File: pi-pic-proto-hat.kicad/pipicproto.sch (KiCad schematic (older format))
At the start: 27 parts, among them J1 RUN/~PGM~, J10 Conn_01x13_Male, J2 Conn_SW1, J22 Conn_01x13_Male, J3 Conn_01x05_Male, J6 Barrel_Jack_Switch, J7 Conn_01x24_Male, J8 Conn_01x06_Male, J9 Conn_01x02_Male, P1 Conn_02x20_Odd_Even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

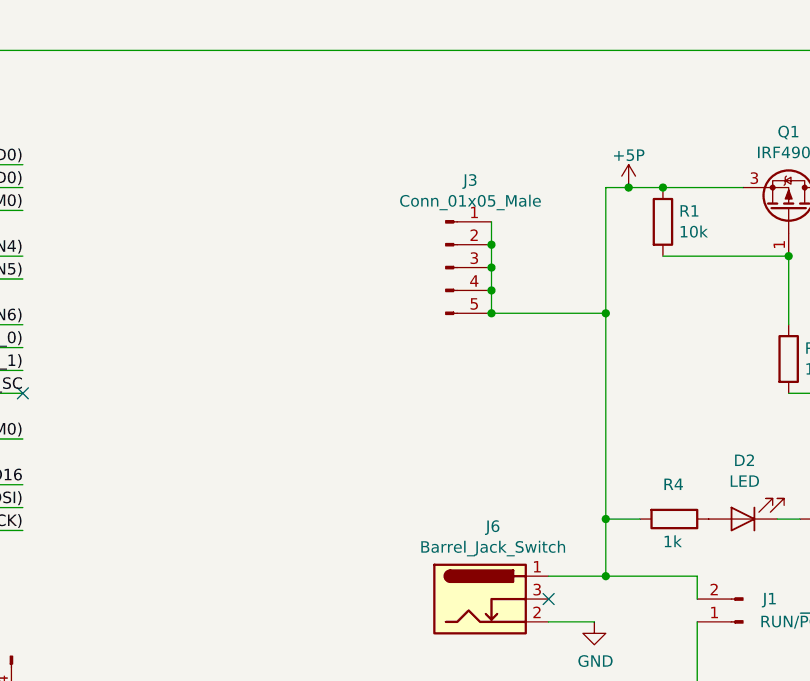
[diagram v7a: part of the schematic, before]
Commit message: V2.16: added regulator and connector for +3V3P (3V3 permanently on)
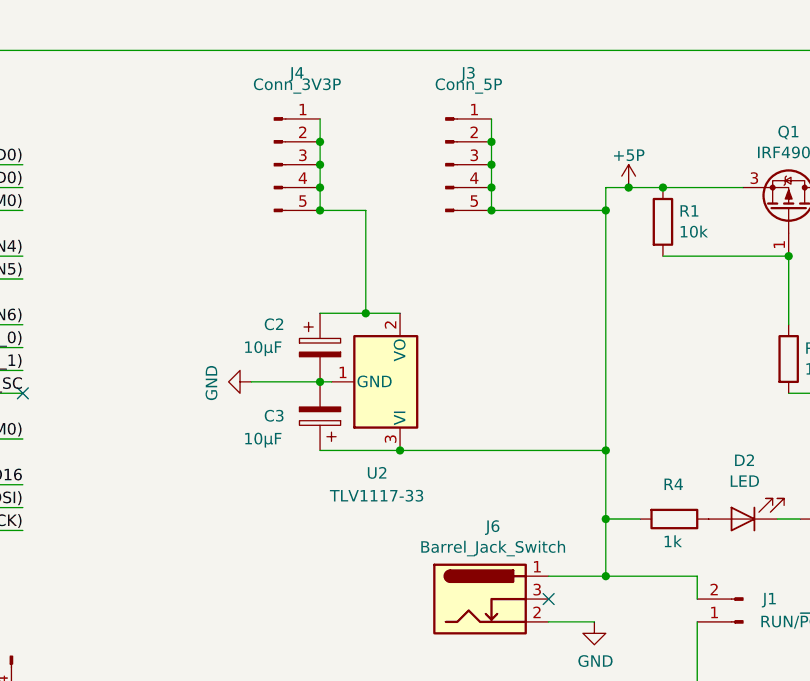
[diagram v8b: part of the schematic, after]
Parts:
- added C2, C3: 10µF, Capacitor_Tantalum_SMD:CP_EIA-3216-18_Kemet-A, symbol Device:CP
- added J4: Conn_3V3P, Connector_PinHeader_2.54mm:PinHeader_1x05_P2.54mm_Vertical, symbol Connector:Conn_01x05_Male
- added U2: TLV1117-33, Package_TO_SOT_SMD:SOT-223, symbol Regulator_Linear:TLV1117-33
- J3: value Conn_01x05_Male -> Conn_5P
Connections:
- net +5P: now also C3.1, U2.3 (VI)
- net GND: now also C2.2, C3.2, U2.1 (GND)
- new net: C2.1, J4.1 (Pin_1), J4.2 (Pin_2), J4.3 (Pin_3), J4.4 (Pin_4), J4.5 (Pin_5), U2.2 (VO)
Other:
- moved on the sheet: J3
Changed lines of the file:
@@
 Title "PI PIC Prototyping Area"
 Date "2020-07-24"
-Rev "2.15"
+Rev "2.16"
 Comp "Bernhard Bablok, Lothar Hiller"
 Comment1 "https://github.com/bablokb/pi-pic-proto-hat"
@@
 	6900 3400 6900 4300
 Wire Wire Line
-	6500 1500 6500 2050
+	6500 1500 6500 1600
 Wire Wire Line
 	6500 3200 6900 3200
@@
 L Connector:Conn_01x05_Male J3
 U 1 1 5F1C34FF
-P 5800 1850
-F 0 "J3" H 5908 2231 50  0000 C CNN
-F 1 "Conn_01x05_Male" H 5908 2140 50  0000 C CNN
-F 2 "Connector_PinHeader_2.54mm:PinHeader_1x05_P2.54mm_Vertical" H 5800 1850 50  0001 C CNN
-F 3 "~" H 5800 1850 50  0001 C CNN
-	1    5800 1850
-	1    0    0    -1
-$EndComp
-Wire Wire Line
-	6500 2050 6000 2050
-Wire Wire Line
-	6000 2050 6000 1950
-Connection ~ 6500 2050
-Wire Wire Line
-	6500 2050 6500 2950
-Connection ~ 6000 2050
-Wire Wire Line
-	6000 1850 6000 1750
-Wire Wire Line
-	6000 1950 6000 1850
-Connection ~ 6000 1950
-Connection ~ 6000 1850
-Wire Wire Line
-	6000 1750 6000 1650
-Connection ~ 6000 1750
+P 5800 1400
+F 0 "J3" H 5900 1800 50  0000 C CNN
+F 1 "Conn_5P" H 5900 1750 50  0000 C CNN
+F 2 "Connector_PinHeader_2.54mm:PinHeader_1x05_P2.54mm_Vertical" H 5800 1400 50  0001 C CNN
+F 3 "~" H 5800 1400 50  0001 C CNN
+	1    5800 1400
+	1    0    0    -1
+$EndComp
+Wire Wire Line
+	6500 1600 6000 1600
+Wire Wire Line
+	6000 1600 6000 1500
+Connection ~ 6000 1600
+Wire Wire Line
+	6000 1400 6000 1300
+Wire Wire Line
+	6000 1500 6000 1400
+Connection ~ 6000 1500
+Connection ~ 6000 1400
+Wire Wire Line
+	6000 1300 6000 1200
+Connection ~ 6000 1300
+$Comp
+L power:GND #PWR09
+U 1 1 5F1C3E14
+P 4950 2350
+F 0 "#PWR09" H 4950 2100 50  0001 C CNN
+F 1 "GND" H 4955 2177 50  0000 C CNN
+F 2 "" H 4950 2350 50  0001 C CNN
+F 3 "" H 4950 2350 50  0001 C CNN
+	1    4950 2350
+	0    1    1    0
+$EndComp
+Wire Wire Line
+	5300 2350 5250 2350
+$Comp
+L Device:CP C2
+U 1 1 5F1C3E1B
+P 5250 2200
+F 0 "C2" H 5050 2300 50  0000 C CNN
+F 1 "10µF" H 5000 2200 50  0000 C CNN
+F 2 "Capacitor_Tantalum_SMD:CP_EIA-3216-18_Kemet-A" H 5288 2050 50  0001 C CNN
+F 3 "~" H 5250 2200 50  0001 C CNN
+	1    5250 2200
+	1    0    0    -1
+$EndComp
+Connection ~ 5250 2350
+Wire Wire Line
+	5250 2350 4950 2350
+$Comp
+L Device:CP C3
+U 1 1 5F1C3E29
+P 5250 2500
+F 0 "C3" H 5450 2500 50  0000 C CNN
+F 1 "10µF" H 5500 2600 50  0000 C CNN
+F 2 "Capacitor_Tantalum_SMD:CP_EIA-3216-18_Kemet-A" H 5288 2350 50  0001 C CNN
+F 3 "~" H 5250 2500 50  0001 C CNN
+	1    5250 2500
+	-1   0    0    1
+$EndComp
+Wire Wire Line
+	5250 2050 5450 2050
+Connection ~ 6500 1600
+Wire Wire Line
+	6500 1600 6500 2650
+Connection ~ 6500 2650
+Wire Wire Line
+	6500 2650 6500 2950
+$Comp
+L Connector:Conn_01x05_Male J4
+U 1 1 5F1D5F8D
+P 5050 1400
+F 0 "J4" H 5150 1800 50  0000 C CNN
+F 1 "Conn_3V3P" H 5150 1750 50  0000 C CNN
+F 2 "Connector_PinHeader_2.54mm:PinHeader_1x05_P2.54mm_Vertical" H 5050 1400 50  0001 C CNN
+F 3 "~" H 5050 1400 50  0001 C CNN
+	1    5050 1400
+	1    0    0    -1
+$EndComp
+Wire Wire Line
+	5450 2050 5450 1600
+Wire Wire Line
+	5450 1600 5250 1600
+Connection ~ 5450 2050
+Wire Wire Line
+	5450 2050 5600 2050
+Wire Wire Line
+	5250 1600 5250 1500
+Connection ~ 5250 1600
+Wire Wire Line
+	5250 1500 5250 1400
+Connection ~ 5250 1500
+Wire Wire Line
+	5250 1400 5250 1300
+Connection ~ 5250 1400
+Wire Wire Line
+	5250 1300 5250 1200
+Connection ~ 5250 1300
+Connection ~ 5600 2650
+Wire Wire Line
+	5600 2650 6500 2650
+Wire Wire Line
+	5250 2650 5600 2650
+$Comp
+L Regulator_Linear:TLV1117-33 U2
+U 1 1 5F1C3E21
+P 5600 2350
+F 0 "U2" V 5200 2250 50  0000 C CNN
+F 1 "TLV1117-33" V 5100 2250 50  0000 C CNN
+F 2 "Package_TO_SOT_SMD:SOT-223" H 5600 2350 50  0001 C CNN
+F 3 "http://www.ti.com/lit/ds/symlink/tlv1117.pdf" H 5600 2350 50  0001 C CNN
+	1    5600 2350
+	0    1    -1   0
+$EndComp
 $EndSCHEMATC
